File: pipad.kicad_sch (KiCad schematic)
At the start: 2 parts

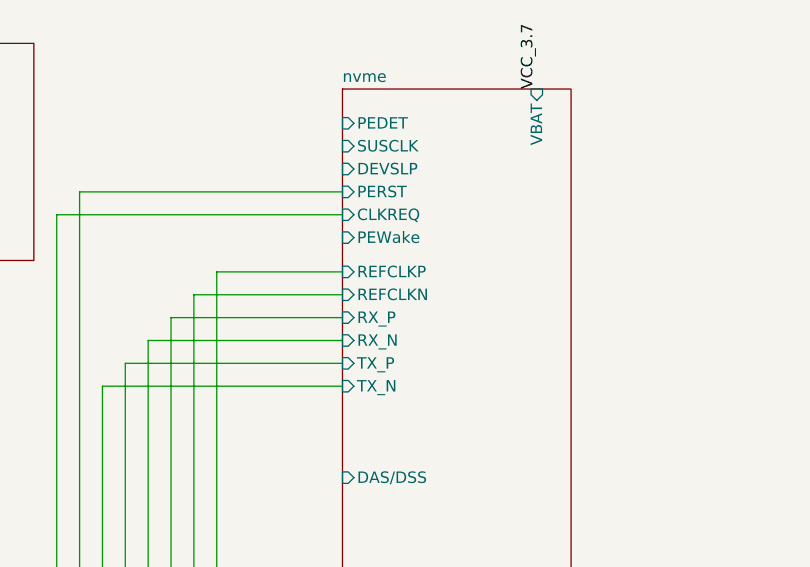
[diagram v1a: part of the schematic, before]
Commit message: Route DSI signals. Also fix the schematic for the touchscreen connectors, which got messed up somehow.
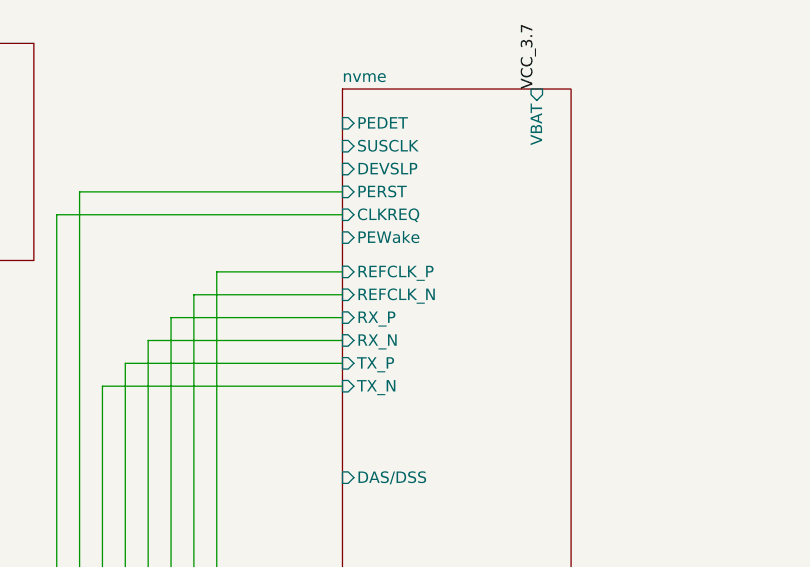
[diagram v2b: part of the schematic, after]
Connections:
- net nvme/REFCLKN renamed nvme/REFCLK_N
- net nvme/REFCLKP renamed nvme/REFCLK_P
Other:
- sheet nvme ports: added REFCLK_N, REFCLK_P; removed REFCLKN, REFCLKP
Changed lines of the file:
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@@
       (effects (font (size 1.27 1.27)) (justify left))
     )
-    (pin "REFCLKN" input (at 269.24 82.55 180)
+    (pin "REFCLK_N" input (at 269.24 82.55 180)
       (effects (font (size 1.27 1.27)) (justify left))
     )
-    (pin "REFCLKP" input (at 269.24 80.01 180)
+    (pin "REFCLK_P" input (at 269.24 80.01 180)
       (effects (font (size 1.27 1.27)) (justify left))
     )

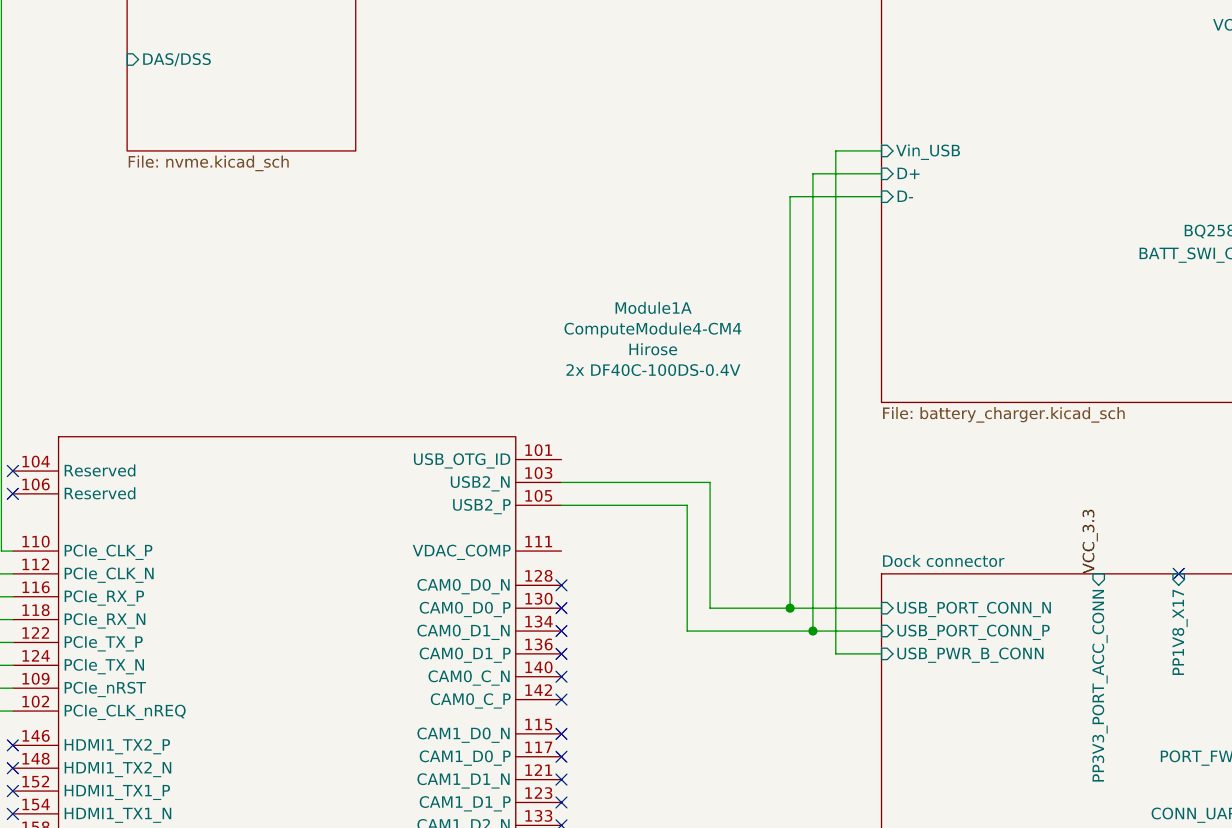
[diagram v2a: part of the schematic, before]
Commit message: Lots of changes: add USB switch in charger circuit, reroute differential pairs using proper track widths; make CM4 courtyard the full size. Fixes #11.
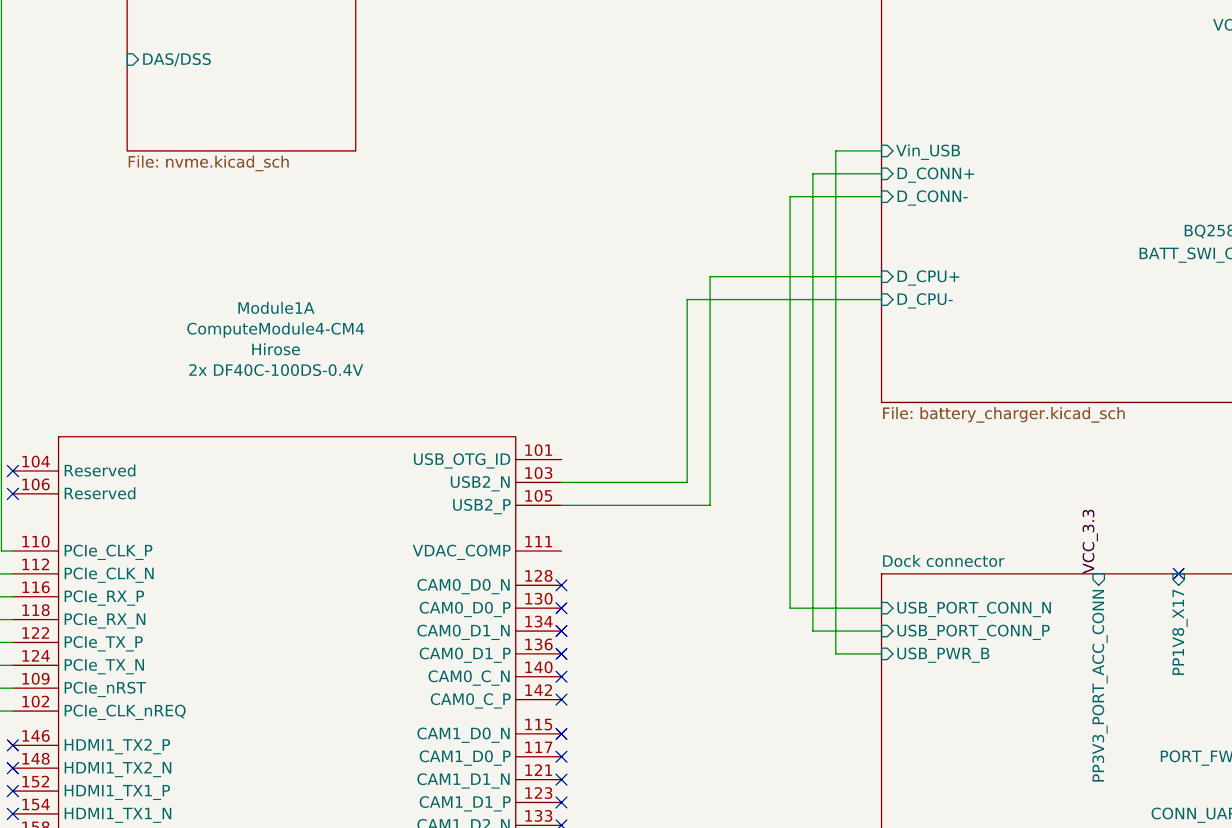
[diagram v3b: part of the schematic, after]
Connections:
- net Battery charger/D+ renamed Battery charger/D_CPU+
- net Battery charger/D- renamed Battery charger/D_CPU-
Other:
- sheet Battery charger ports: added D_CONN+, D_CONN-, D_CPU+, D_CPU-; removed D+, D-
- sheet Dock connector ports: added USB_PWR_B; removed USB_PWR_B_CONN
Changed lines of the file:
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@@
   (junction (at 317.5 256.54) (diameter 1.016) (color 0 0 0 0))
   (junction (at 317.5 259.08) (diameter 1.016) (color 0 0 0 0))
-  (junction (at 342.9 163.83) (diameter 1.016) (color 0 0 0 0))
-  (junction (at 345.44 166.37) (diameter 1.016) (color 0 0 0 0))
   (junction (at 349.25 248.92) (diameter 1.016) (color 0 0 0 0))
   (no_connect (at 154.94 148.59))
@@
     (stroke (width 0) (type solid) (color 0 0 0 0))
   )
-  (wire (pts (xy 317.5 149.86) (xy 334.01 149.86))
+  (wire (pts (xy 317.5 152.4) (xy 334.01 152.4))
     (stroke (width 0) (type solid) (color 0 0 0 0))
   )
@@
     (stroke (width 0) (type solid) (color 0 0 0 0))
   )
-  (wire (pts (xy 331.47 152.4) (xy 317.5 152.4))
-    (stroke (width 0) (type solid) (color 0 0 0 0))
-  )
-  (wire (pts (xy 331.47 166.37) (xy 331.47 152.4))
-    (stroke (width 0) (type solid) (color 0 0 0 0))
-  )
-  (wire (pts (xy 334.01 149.86) (xy 334.01 163.83))
-    (stroke (width 0) (type solid) (color 0 0 0 0))
-  )
-  (wire (pts (xy 334.01 163.83) (xy 342.9 163.83))
+  (wire (pts (xy 331.47 129.54) (xy 331.47 149.86))
+    (stroke (width 0) (type solid) (color 0 0 0 0))
+  )
+  (wire (pts (xy 331.47 149.86) (xy 317.5 149.86))
+    (stroke (width 0) (type solid) (color 0 0 0 0))
+  )
+  (wire (pts (xy 334.01 127) (xy 353.06 127))
+    (stroke (width 0) (type solid) (color 0 0 0 0))
+  )
+  (wire (pts (xy 334.01 152.4) (xy 334.01 127))
     (stroke (width 0) (type solid) (color 0 0 0 0))
   )
@@
     (stroke (width 0) (type solid) (color 0 0 0 0))
   )
-  (wire (pts (xy 345.44 166.37) (xy 331.47 166.37))
-    (stroke (width 0) (type solid) (color 0 0 0 0))
-  )
   (wire (pts (xy 347.98 113.03) (xy 353.06 113.03))
     (stroke (width 0) (type solid) (color 0 0 0 0))
@@
   )
   (wire (pts (xy 353.06 118.11) (xy 342.9 118.11))
+    (stroke (width 0) (type solid) (color 0 0 0 0))
+  )
+  (wire (pts (xy 353.06 129.54) (xy 331.47 129.54))
     (stroke (width 0) (type solid) (color 0 0 0 0))
   )
@@
   )
   (symbol (lib_id "CM4IO:ComputeModule4-CM4") (at 187.96 201.93 0) (unit 1)
-    (in_bom yes) (on_board yes) (fields_autoplaced)
-    (property "Reference" "Module1" (id 0) (at 327.66 130.5264 0))
-    (property "Value" "ComputeModule4-CM4" (id 1) (at 327.66 132.8251 0))
+    (in_bom yes) (on_board yes)
+    (property "Reference" "Module1" (id 0) (at 285.75 130.5264 0))
+    (property "Value" "ComputeModule4-CM4" (id 1) (at 285.75 132.8251 0))
     (property "Footprint" "footprints:Raspberry-Pi-4-Compute-Module" (id 2) (at 330.2 228.6 0)
       (effects (font (size 1.27 1.27)) hide)
@@
       (effects (font (size 1.27 1.27)) hide)
     )
-    (property "Field4" "Hirose" (id 4) (at 327.66 135.1238 0))
-    (property "Field5" "2x DF40C-100DS-0.4V" (id 5) (at 327.66 137.4225 0))
+    (property "Field4" "Hirose" (id 4) (at 285.75 135.1238 0))
+    (property "Field5" "2x DF40C-100DS-0.4V" (id 5) (at 285.75 137.4225 0))
     (pin "1")
     (pin "10")
@@
       (effects (font (size 1.27 1.27)) (justify left top))
     )
-    (pin "D+" input (at 353.06 115.57 180)
-      (effects (font (size 1.27 1.27)) (justify left))
-    )
-    (pin "D-" input (at 353.06 118.11 180)
+    (pin "D_CONN+" input (at 353.06 115.57 180)
+      (effects (font (size 1.27 1.27)) (justify left))
+    )
+    (pin "D_CONN-" input (at 353.06 118.11 180)
       (effects (font (size 1.27 1.27)) (justify left))
     )
@@
     (pin "VOUT_3.7" output (at 400.05 99.06 0)
       (effects (font (size 1.27 1.27)) (justify right))
+    )
+    (pin "D_CPU+" input (at 353.06 127 180)
+      (effects (font (size 1.27 1.27)) (justify left))
+    )
+    (pin "D_CPU-" input (at 353.06 129.54 180)
+      (effects (font (size 1.27 1.27)) (justify left))
     )
   )
@@
       (effects (font (size 1.27 1.27)) (justify left top))
     )
-    (pin "USB_PWR_B_CONN" input (at 353.06 168.91 180)
+    (pin "USB_PWR_B" input (at 353.06 168.91 180)
       (effects (font (size 1.27 1.27)) (justify left))
     )
@@
       (reference "U3") (unit 1) (value "TPA2006D1DRBR") (footprint "footprints:TPA2006D1DRBR")
     )
+    (path "/4ecc04d7-c0c4-4778-83ba-d295a895ebe9/94492ea8-d843-4fc7-a45f-b0b96f4d35ea"
+      (reference "#PWR01") (unit 1) (value "GND") (footprint "")
+    )
     (path "/4ecc04d7-c0c4-4778-83ba-d295a895ebe9/00000000-0000-0000-0000-00006042f1b0"
       (reference "#PWR05") (unit 1) (value "GND") (footprint "")
@@
       (reference "C27") (unit 1) (value "2.2uF") (footprint "Capacitor_SMD:C_0402_1005Metric")
     )
+    (path "/4ecc04d7-c0c4-4778-83ba-d295a895ebe9/a99d7e68-909f-481f-8e33-bbd85d2949d1"
+      (reference "C55") (unit 1) (value "2.2uF") (footprint "Capacitor_SMD:C_0402_1005Metric")
+    )
     (path "/4ecc04d7-c0c4-4778-83ba-d295a895ebe9/00000000-0000-0000-0000-000060028f7a"
       (reference "J6") (unit 1) (value "504740-5100") (footprint "footprints:504740-5100")
@@
       (reference "#PWR0138") (unit 1) (value "GND") (footprint "")
     )
+    (path "/eed4aa3c-bec9-4438-9bbd-324cd17b6734/929791e3-0750-4213-981d-f865b5b5b85b"
+      (reference "#PWR0142") (unit 1) (value "GND") (footprint "")
+    )
+    (path "/eed4aa3c-bec9-4438-9bbd-324cd17b6734/fbdd2f42-b3e3-4a64-8ee4-5ff3015d0ffa"
+      (reference "#PWR0143") (unit 1) (value "GND") (footprint "")
+    )
     (path "/eed4aa3c-bec9-4438-9bbd-324cd17b6734/00000000-0000-0000-0000-00005f7967cf"
       (reference "C47") (unit 1) (value "1.0uF") (footprint "Capacitor_SMD:C_0402_1005Metric")
@@
       (reference "C53") (unit 1) (value "22uF") (footprint "Capacitor_SMD:C_0805_2012Metric")
     )
-    (path "/eed4aa3c-bec9-4438-9bbd-324cd17b6734/1bc13c2e-0559-4397-af60-bae459a7c618"
-      (reference "D2") (unit 1) (value "D_Schottky") (footprint "footprints:NSR10F20NXT5G")
-    )
     (path "/eed4aa3c-bec9-4438-9bbd-324cd17b6734/80125fd9-cbee-474e-bd31-4c8328a3ee11"
       (reference "J8") (unit 1) (value "Conn_01x04") (footprint "footprints:ipad battery connector")
@@
       (reference "R21") (unit 1) (value "30.1k") (footprint "Resistor_SMD:R_0402_1005Metric")
     )
+    (path "/eed4aa3c-bec9-4438-9bbd-324cd17b6734/9adb0005-283c-4b18-82d8-133b5b8bd953"
+      (reference "R22") (unit 1) (value "10k") (footprint "Resistor_SMD:R_0402_1005Metric")
+    )
     (path "/eed4aa3c-bec9-4438-9bbd-324cd17b6734/00000000-0000-0000-0000-00005fc06d49"
       (reference "TP1") (unit 1) (value "DNP") (footprint "TestPoint:TestPoint_Pad_1.0x1.0mm")
@@
       (reference "TP2") (unit 1) (value "DNP") (footprint "TestPoint:TestPoint_Pad_1.0x1.0mm")
     )
-    (path "/eed4aa3c-bec9-4438-9bbd-324cd17b6734/00000000-0000-0000-0000-00005fa0fc37"
-      (reference "TP3") (unit 1) (value "DNP") (footprint "TestPoint:TestPoint_Pad_1.0x1.0mm")
-    )
     (path "/eed4aa3c-bec9-4438-9bbd-324cd17b6734/38595104-6517-44f7-a6c6-d538e4067cd5"
-      (reference "TP5") (unit 1) (value "TestPoint") (footprint "")
+      (reference "TP5") (unit 1) (value "TestPoint") (footprint "TestPoint:TestPoint_Pad_D1.0mm")
     )
     (path "/eed4aa3c-bec9-4438-9bbd-324cd17b6734/00000000-0000-0000-0000-00005f798394"
       (reference "U15") (unit 1) (value "BQ25895RTW") (footprint "footprints:Texas_S-PWQFN-N24_EP2.7x2.7mm_ThermalVias")
     )
+    (path "/eed4aa3c-bec9-4438-9bbd-324cd17b6734/e914ae85-9fa3-4103-9d2c-d0b470367bbc"
+      (reference "U17") (unit 1) (value "NX3DV42GU") (footprint "footprints:NX3DV42GU")
+    )
     (path "/593f2d4b-248b-4b7c-ad0b-1e77412a278c/2e77eb4f-b196-41c9-89cb-0d614cc04886"

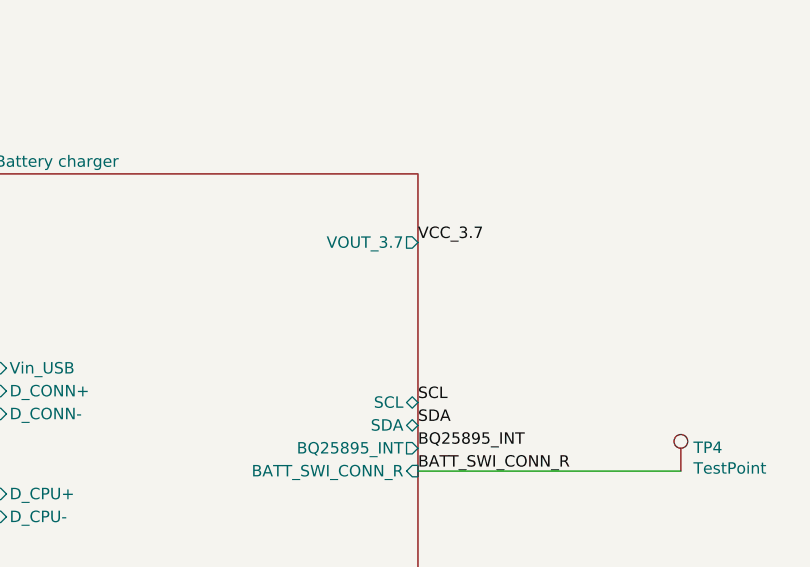
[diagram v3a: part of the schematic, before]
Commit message: reroute LVDS diff pairs; add 5v boost converter. Fixes #1.
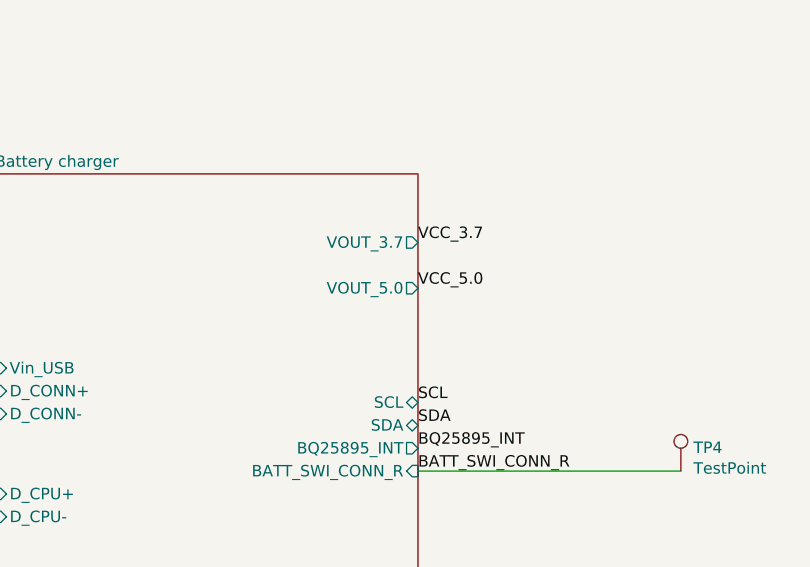
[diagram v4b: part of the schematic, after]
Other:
- sheet Battery charger ports: added VOUT_5.0; removed none
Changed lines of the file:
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@@
+    (effects (font (size 1.27 1.27)) (justify left bottom))
+  )
+  (label "VCC_5.0" (at 400.05 104.14 0)
     (effects (font (size 1.27 1.27)) (justify left bottom))
   )
@@
       (effects (font (size 1.27 1.27)) (justify left))
     )
+    (pin "VOUT_5.0" output (at 400.05 104.14 0)
+      (effects (font (size 1.27 1.27)) (justify right))
+    )
   )
   (sheet (at 353.06 160.02) (size 49.53 93.98) (fields_autoplaced)
@@
       (reference "J9") (unit 1) (value "Conn_01x34_Female") (footprint "footprints:20474-030E-11")
     )
+    (path "/1cd8b29a-6edd-403b-84dd-3cf97c71d81a/6f873648-ff3d-4c25-9fca-3036d0d88c8a"
+      (reference "JP3") (unit 1) (value "Jumper_NC_Small") (footprint "Resistor_SMD:R_0402_1005Metric")
+    )
     (path "/1cd8b29a-6edd-403b-84dd-3cf97c71d81a/e043cedd-01c1-42d0-b9c5-2811df027170"
       (reference "L1") (unit 1) (value "4.7uH") (footprint "Inductor_SMD:L_0805_2012Metric")
@@
       (reference "#FLG0104") (unit 1) (value "PWR_FLAG") (footprint "")
     )
+    (path "/eed4aa3c-bec9-4438-9bbd-324cd17b6734/c838ec75-5556-4a35-8997-014a49ed61d5"
+      (reference "#PWR03") (unit 1) (value "GND") (footprint "")
+    )
+    (path "/eed4aa3c-bec9-4438-9bbd-324cd17b6734/5ac0ff9b-d8c8-42e2-86d8-bb6d1abf9381"
+      (reference "#PWR018") (unit 1) (value "GND") (footprint "")
+    )
+    (path "/eed4aa3c-bec9-4438-9bbd-324cd17b6734/62d1699b-aeb7-4562-b3e5-cb552d8a6b68"
+      (reference "#PWR038") (unit 1) (value "GND") (footprint "")
+    )
+    (path "/eed4aa3c-bec9-4438-9bbd-324cd17b6734/2a748189-f179-4a65-a569-8d9d8f422180"
+      (reference "#PWR041") (unit 1) (value "GND") (footprint "")
+    )
     (path "/eed4aa3c-bec9-4438-9bbd-324cd17b6734/b7269330-1a8b-4d32-8cbf-f9de4c1809fa"
       (reference "#PWR0124") (unit 1) (value "GND") (footprint "")
@@
       (reference "C53") (unit 1) (value "22uF") (footprint "Capacitor_SMD:C_0805_2012Metric")
     )
+    (path "/eed4aa3c-bec9-4438-9bbd-324cd17b6734/c08f2455-e237-4af6-aec0-d1ea3349686b"
+      (reference "C56") (unit 1) (value "22uF") (footprint "Capacitor_SMD:C_0805_2012Metric")
+    )
+    (path "/eed4aa3c-bec9-4438-9bbd-324cd17b6734/22528d77-c980-45a1-83a2-597121e4c311"
+      (reference "C57") (unit 1) (value "22uF") (footprint "Capacitor_SMD:C_0805_2012Metric")
+    )
+    (path "/eed4aa3c-bec9-4438-9bbd-324cd17b6734/39a9968f-5240-440b-9bcd-438448f19110"
+      (reference "C58") (unit 1) (value "22uF") (footprint "Capacitor_SMD:C_0805_2012Metric")
+    )
+    (path "/eed4aa3c-bec9-4438-9bbd-324cd17b6734/f05170eb-73f0-4ad8-baf9-51c5ed4cf650"
+      (reference "C59") (unit 1) (value "22uF") (footprint "Capacitor_SMD:C_0805_2012Metric")
+    )
     (path "/eed4aa3c-bec9-4438-9bbd-324cd17b6734/80125fd9-cbee-474e-bd31-4c8328a3ee11"
       (reference "J8") (unit 1) (value "Conn_01x04") (footprint "footprints:ipad battery connector")
@@
       (reference "JP4") (unit 1) (value "SolderJumper_2_Open") (footprint "Resistor_SMD:R_0402_1005Metric")
     )
+    (path "/eed4aa3c-bec9-4438-9bbd-324cd17b6734/b307863c-6ee2-4270-92c4-af306c3bc135"
+      (reference "JP5") (unit 1) (value "Jumper_NC_Small") (footprint "Resistor_SMD:R_0402_1005Metric")
+    )
     (path "/eed4aa3c-bec9-4438-9bbd-324cd17b6734/00000000-0000-0000-0000-00005f795446"
       (reference "L2") (unit 1) (value "2.2uH") (footprint "Inductor_SMD:L_1008_2520Metric")
     )
+    (path "/eed4aa3c-bec9-4438-9bbd-324cd17b6734/a046568b-42d0-4a9f-87e1-7868ad902963"
+      (reference "L3") (unit 1) (value "2.2uH") (footprint "Inductor_SMD:L_1008_2520Metric")
+    )
     (path "/eed4aa3c-bec9-4438-9bbd-324cd17b6734/00000000-0000-0000-0000-00005f78f911"
       (reference "R19") (unit 1) (value "220") (footprint "Resistor_SMD:R_0402_1005Metric")
@@
       (reference "R22") (unit 1) (value "10k") (footprint "Resistor_SMD:R_0402_1005Metric")
     )
+    (path "/eed4aa3c-bec9-4438-9bbd-324cd17b6734/565adb91-6993-45e6-afd5-a698a4ab1e26"
+      (reference "R23") (unit 1) (value "787k") (footprint "Resistor_SMD:R_0402_1005Metric")
+    )
+    (path "/eed4aa3c-bec9-4438-9bbd-324cd17b6734/d7bd6322-e58b-40dd-9c4c-255b2ea54a5c"
+      (reference "R24") (unit 1) (value "150k") (footprint "Resistor_SMD:R_0402_1005Metric")
+    )
     (path "/eed4aa3c-bec9-4438-9bbd-324cd17b6734/00000000-0000-0000-0000-00005fc06d49"
       (reference "TP1") (unit 1) (value "DNP") (footprint "TestPoint:TestPoint_Pad_1.0x1.0mm")
@@
       (reference "U17") (unit 1) (value "NX3DV42GU") (footprint "footprints:NX3DV42GU")
     )
+    (path "/eed4aa3c-bec9-4438-9bbd-324cd17b6734/a416404b-0374-4615-a905-0acc026b6219"
+      (reference "U18") (unit 1) (value "MP3422GG-P") (footprint "footprints:MP3422GG-P")
+    )
     (path "/593f2d4b-248b-4b7c-ad0b-1e77412a278c/2e77eb4f-b196-41c9-89cb-0d614cc04886"
